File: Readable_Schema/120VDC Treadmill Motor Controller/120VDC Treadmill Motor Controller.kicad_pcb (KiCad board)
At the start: 4 copper layers, 186.8 x 133.2 mm, 141 parts, among them J1 TB005-762-03BE, J2 OSTT7020150, J3 TB0011-350-08BE, J4 TB0011-350-08BE, J5 TB0011-350-08BE, J6 TB0011-350-03BE, J7 OSTT7020150, J9 OSTT7020150, K1 T9GV1L14-24, Q1 IPP60R060P7XKSA1, Q2 IPP60R060P7XKSA1, Q3 IPP60R060P7XKSA1, Q4 IPP60R060P7XKSA1, Q5 IPP60R060P7XKSA1, Q7 DN2450N8-G, Q8 VOM1271T, U1 UCC21530DWKR, U2 UCC21530DWKR, U3 TMCS1126B42QDVGRQ1, U4 SN74HCS08DYYR, U5 TPSI3050QDWZRQ1, U6 AMC1311BDWVR

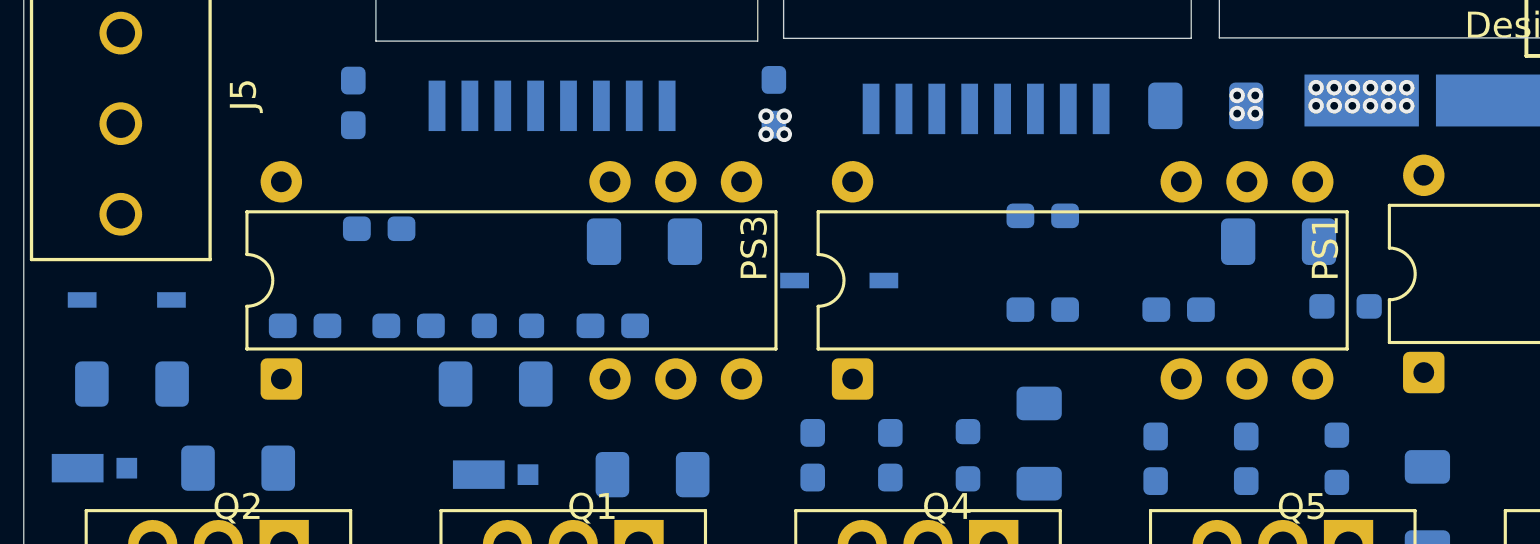
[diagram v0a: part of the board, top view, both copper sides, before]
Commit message: Added a few more fill zones for high power stuff
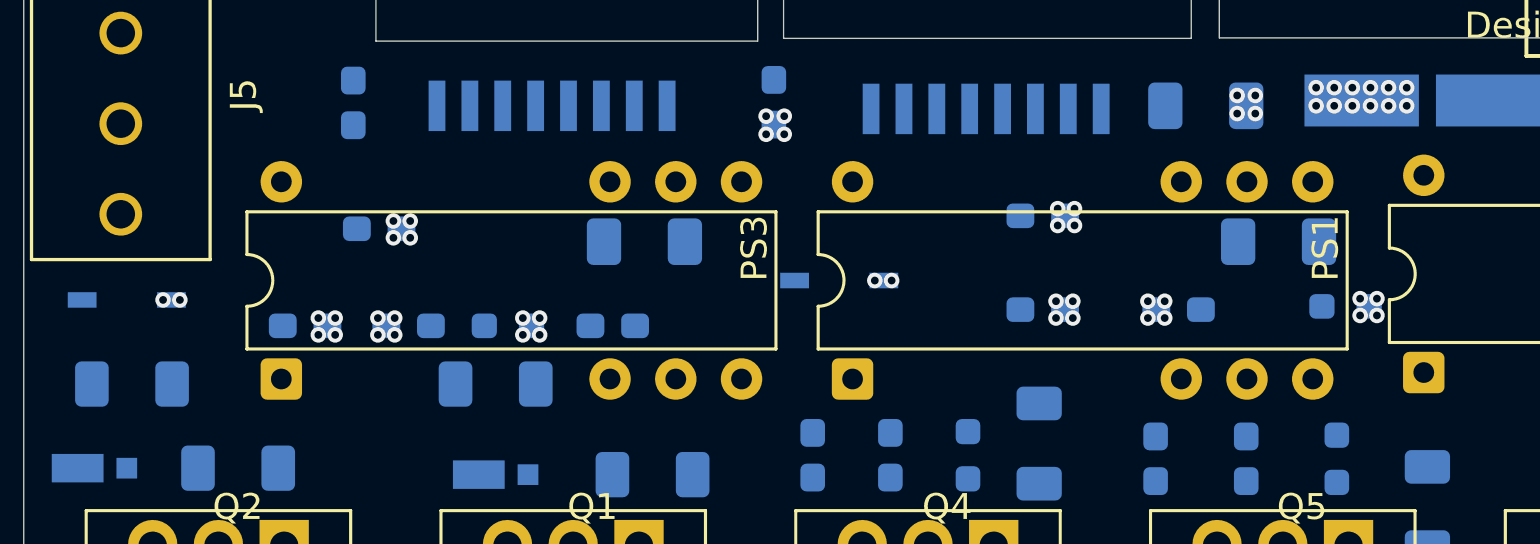
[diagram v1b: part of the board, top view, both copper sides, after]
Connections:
- C15 pad 2: Net-(C15-Pad2) -> Net-(J2-Pin_1)
- C16 pad 1: Net-(C15-Pad2) -> Net-(J2-Pin_1)
- C42 pad 1: Net-(C15-Pad2) -> Net-(J2-Pin_1)
- CR2 pad 1: Net-(C15-Pad2) -> Net-(J2-Pin_1)
- R31 pad 2: Net-(C15-Pad2) -> Net-(J2-Pin_1)
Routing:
- net Net-(J2-Pin_2): vias 0 -> 18
- net Net-(J2-Pin_1): vias 0 -> 18
- added copper zone on In1.Cu, net Net-(J2-Pin_1)
- added copper zone on In1.Cu, net Net-(J2-Pin_2)

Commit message: Continuing fill zones and vias for days, likely a few more hours to wrap up the high voltage side
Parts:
- moved U5 2.30 mm to (79.8, 129.9)
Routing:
- net HV_GND: vias 83 -> 99
- net 170V Rect: vias 0 -> 92
- added copper zone on In1.Cu, net 170V Rect
- added copper zone on In2.Cu, net 170V Rect

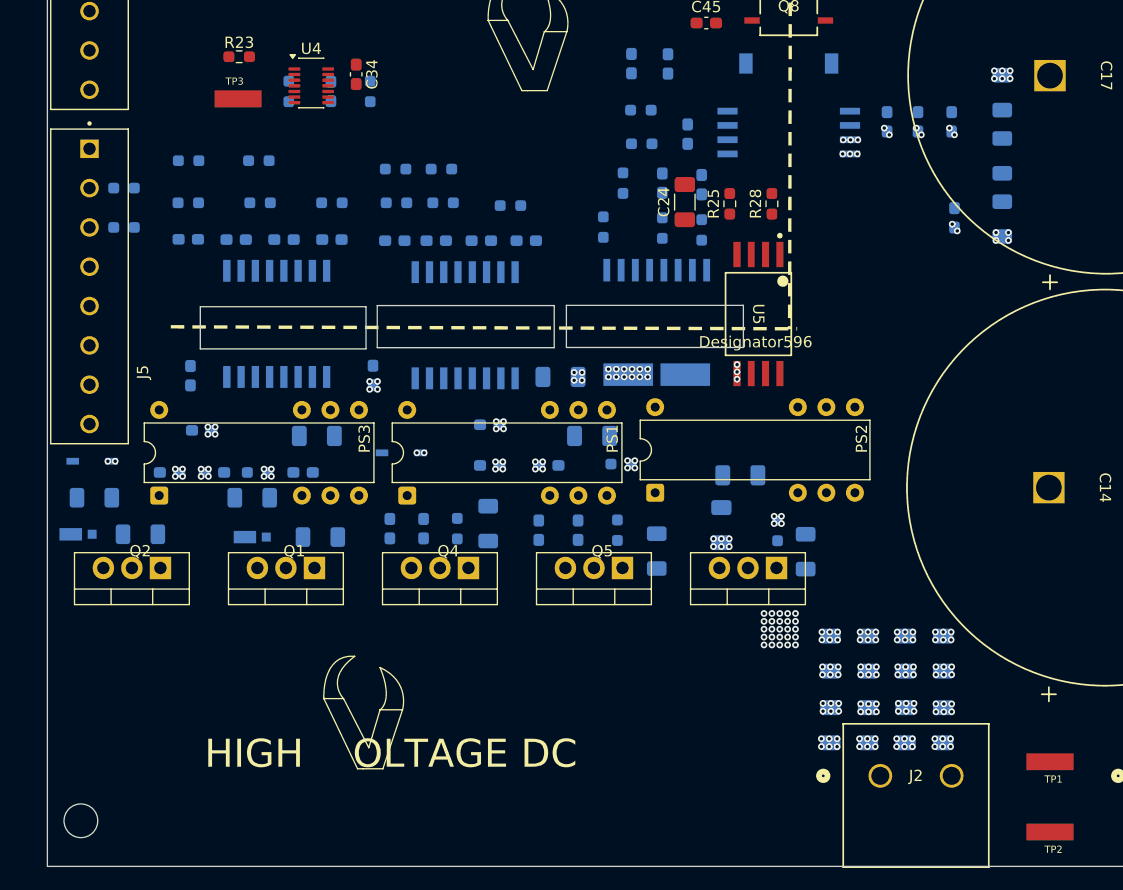
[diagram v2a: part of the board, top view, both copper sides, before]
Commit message: Almost done connecting all the traces on the H bridge side, Sounding like Pete is going to bash on this pretty hard so will likely need to redo all this. Good practice regardless
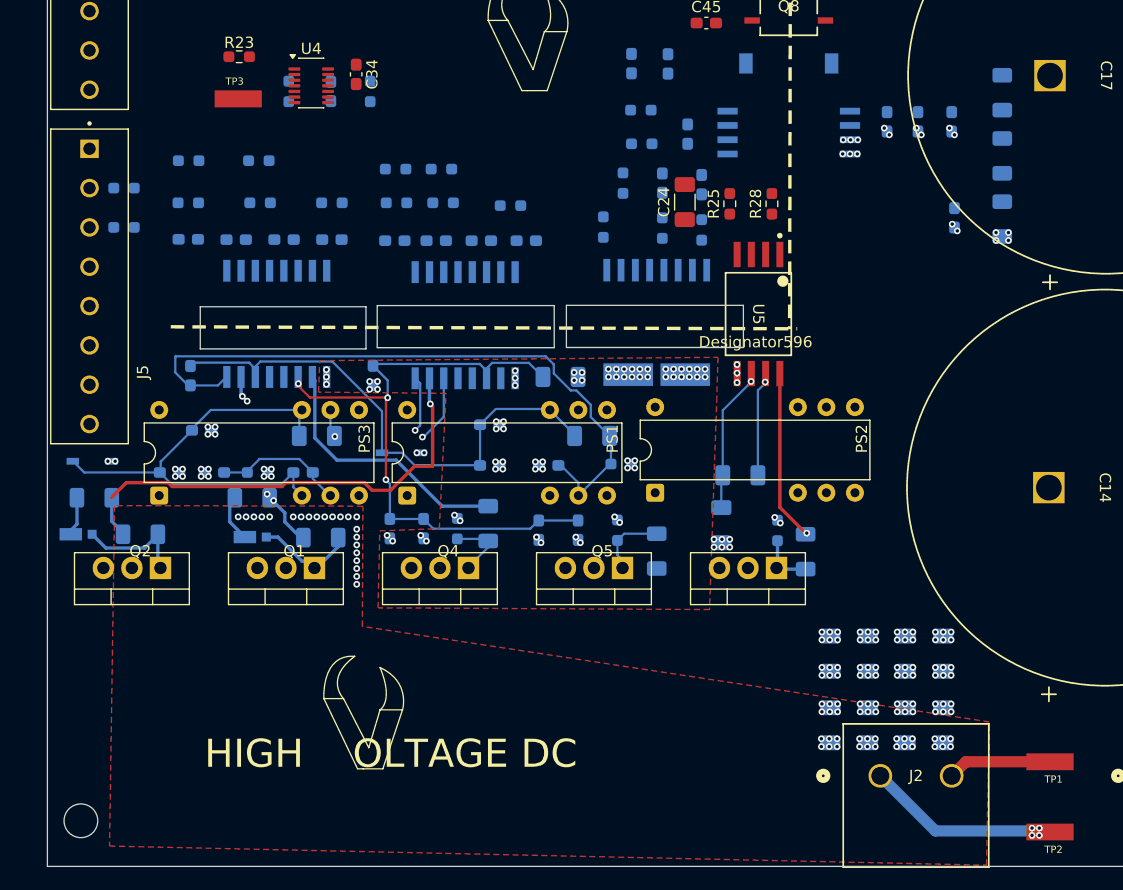
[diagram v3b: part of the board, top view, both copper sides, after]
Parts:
- moved R15 0.06 mm to (40.9, 149.8)
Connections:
- PS1 pad 1: 5v 15w -> unconnected-(PS1-+Vin-Pad1)
- PS1 pad 10: /H_Bridge/hs_ps_1_+ -> unconnected-(PS1-+Vout-Pad10)
- PS1 pad 6: /H_Bridge/hs_ps_1_- -> unconnected-(PS1--Vout-Pad6)
- PS1 pad 8: LV_GND -> unconnected-(PS1--Vin-Pad8)
- PS2 pad 1: 5v 15w -> unconnected-(PS2-+Vin-Pad1)
- PS2 pad 8: LV_GND -> unconnected-(PS2--Vin-Pad8)
- PS3 pad 1: 5v 15w -> unconnected-(PS3-+Vin-Pad1)
- PS3 pad 8: LV_GND -> unconnected-(PS3--Vin-Pad8)
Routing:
- net /H_Bridge/hs_ps_1_+: track 0.00 -> 59.2 mm
- net /H_Bridge/hs_ps_2_-: track 0.00 -> 58.3 mm, vias 0 -> 1
- net /H_Bridge/ls_ps_+: track 0.00 -> 56.7 mm, vias 0 -> 3
- net /H_Bridge/hs_ps_1_-: track 0.00 -> 45.3 mm
- net Net-(U1-OUTA): track 0.00 -> 41.9 mm, vias 0 -> 1
- net /H_Bridge/hs_ps_2_+: track 0.00 -> 26.0 mm, vias 0 -> 2
- net Net-(U2-OUTB): track 0.00 -> 23.3 mm
- net Net-(U2-OUTA): track 0.00 -> 17.0 mm, vias 0 -> 4
- net Net-(J2-Pin_1): track 0.00 -> 15.8 mm, vias 18 -> 22
- net Net-(U5-VDRV): track 0.00 -> 15.3 mm, vias 0 -> 1
- net Net-(U5-VDDM): track 0.00 -> 12.1 mm, vias 0 -> 1
- net Net-(Q3-G): track 0.00 -> 9.47 mm
- net Net-(J2-Pin_2): track 0.00 -> 9.06 mm, vias 18 -> 40
- net Net-(Q2-G): track 0.00 -> 8.60 mm
- net Net-(U5-VDDH): track 0.00 -> 8.57 mm, vias 0 -> 1
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- added copper zone on F.Cu, net /Feedback/in+
- added copper zone on F.Cu, net Net-(J2-Pin_2)

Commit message: worked through a few more low voltage components
finally fixed netclass naming transfer issues by adding to my gitignore
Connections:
- R9 pad 2: 5v 5w -> 5v 15w
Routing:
- net LV_GND: track 0.00 -> 12.7 mm, vias 0 -> 61
- net 5v 15w: vias 0 -> 37
- added copper zone on In1.Cu, net 5v 15w
- added copper zone on In1.Cu, net LV_GND
- added copper zone on In2.Cu, net LV_GND

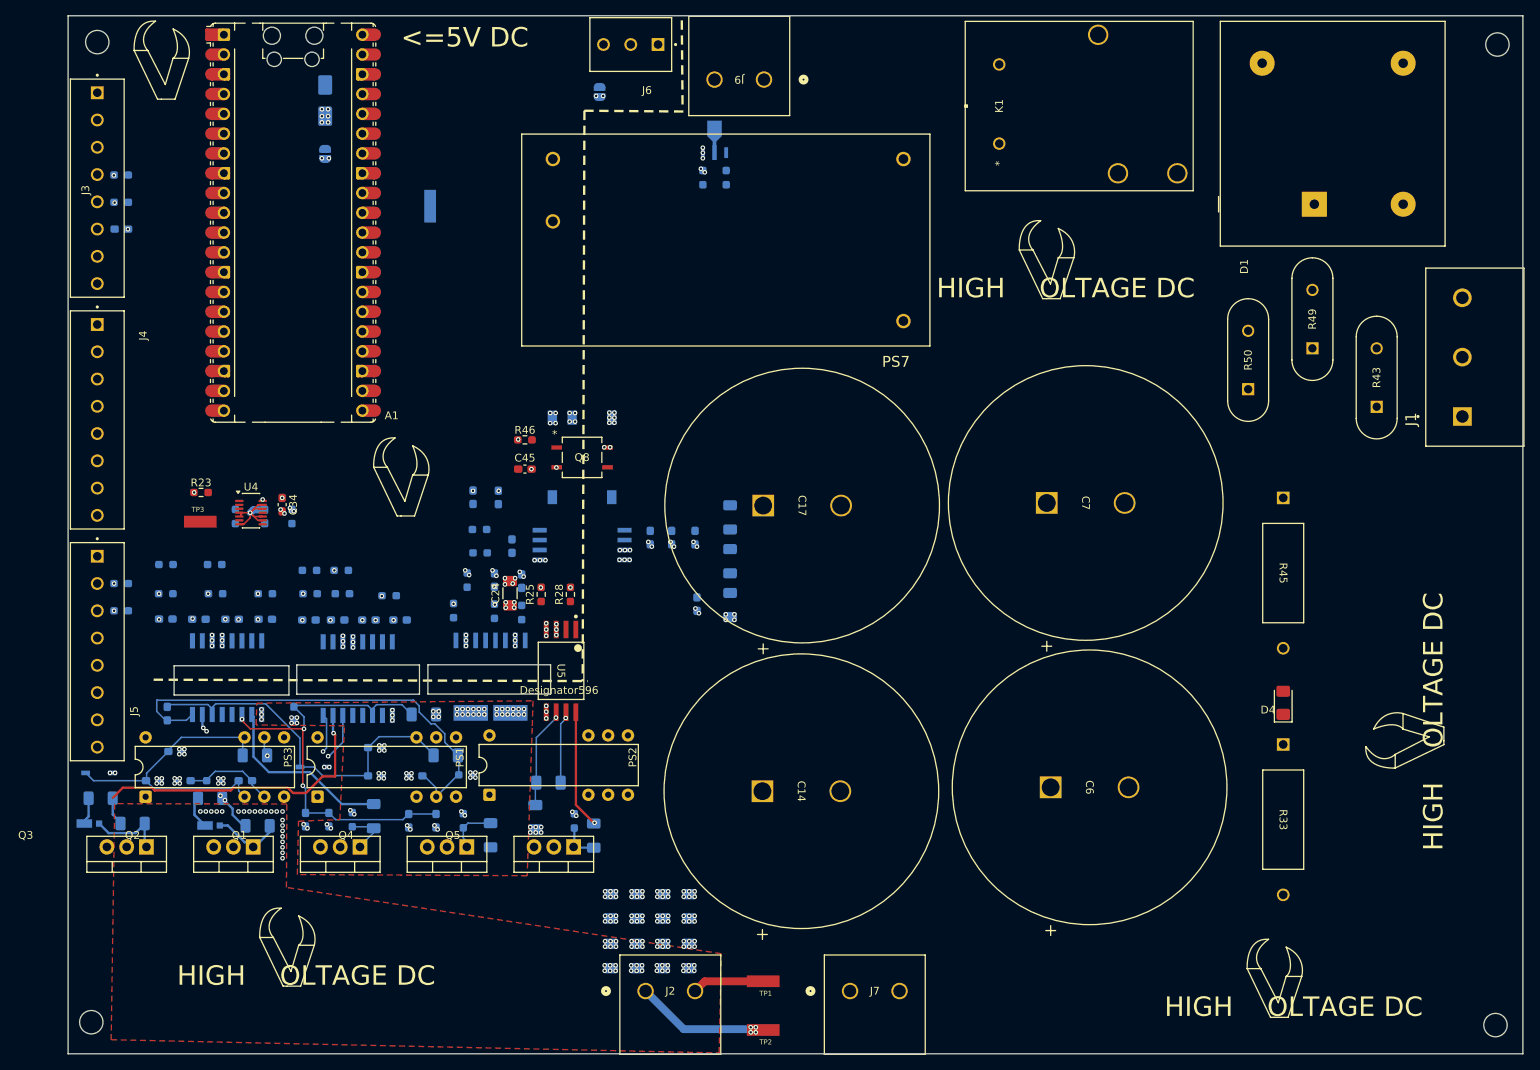
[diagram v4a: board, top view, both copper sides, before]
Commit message: -Still working on traces, working through mostly traces on the low voltage side rather than HV pours like before.
-I'm sure there's a real strategy to these LV traces but I'm not really aware of what that is.

-Will need to go back and clean up a the pours on the HV side
--Add fillets
--proper spacing within same layer
--More room around fet pins to not bottleneck current
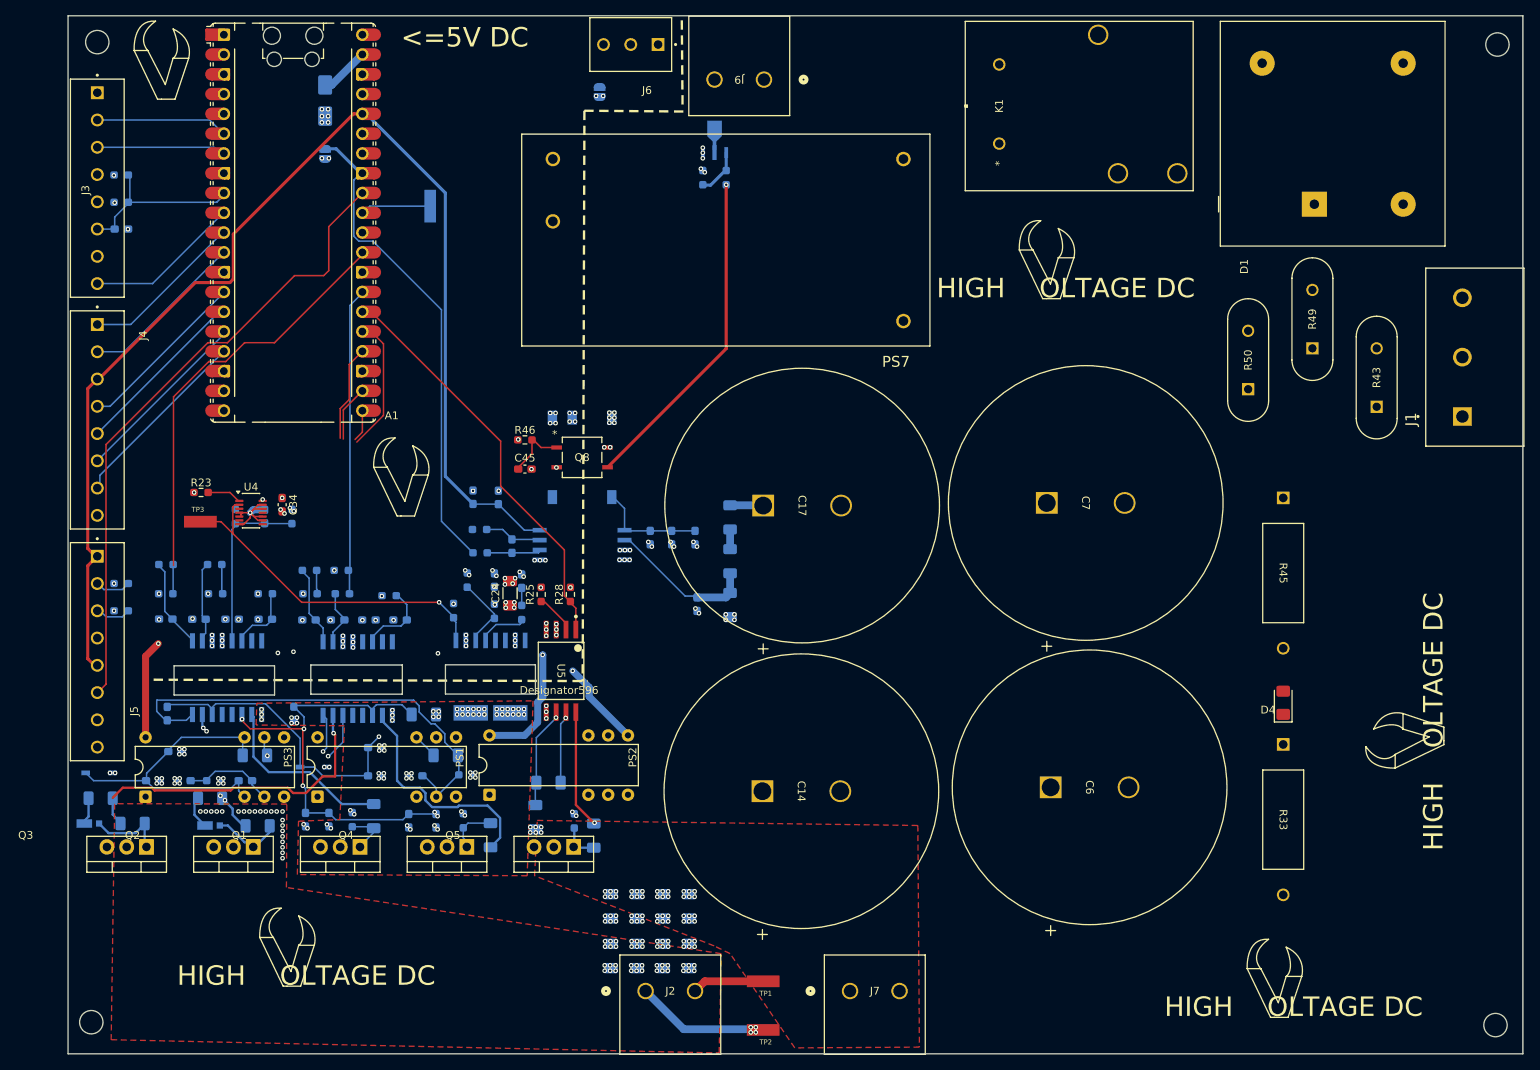
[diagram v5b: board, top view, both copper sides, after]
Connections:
- PS2 pad 10: /H_Bridge/ls_ps_+ -> unconnected-(PS2-+Vout-Pad10)
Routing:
- net 3v3 MCU: track 0.00 -> 156.0 mm
- net Net-(A1-GPIO27_ADC1): track 0.00 -> 81.8 mm
- net /Feedback/adc_gnd: track 0.00 -> 61.8 mm
- net /H_Bridge/pwm_a: track 0.00 -> 57.9 mm
- net /Pi Pico/pre_charge_mcu: track 0.00 -> 52.6 mm
- net /Feedback/OC_out: track 0.00 -> 44.4 mm, vias 0 -> 1
- net Net-(Q8-Pad3): track 0.00 -> 42.6 mm, vias 0 -> 1
- net 5v 15w: track 0.00 -> 40.8 mm, vias 37 -> 40
- net /H_Bridge/dir_a: track 0.00 -> 39.5 mm
- net LV_GND: track 12.7 -> 46.9 mm, vias 61 -> 64
- net Net-(U1-OUTB): track 0.00 -> 28.6 mm
- net /H_Bridge/ls_ps_+: track 56.7 -> 81.3 mm, vias 3 -> 5
- net Net-(A1-GPIO13): track 0.00 -> 23.8 mm
- net Net-(A1-GPIO12): track 0.00 -> 22.9 mm
- net Net-(A1-GPIO11): track 0.00 -> 22.6 mm
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- added copper zone on F.Cu, net Net-(D1-+)
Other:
- outline, holes or cut-outs redrawn
